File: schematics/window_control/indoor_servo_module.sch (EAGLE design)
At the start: 32 parts, among them J1 MTR-SERVO-FS5103B, J2 GND, J3 +5V, J4 OUTDOOR_SIGNAL, J5 J2, J6 J2, J7 J2, Q2 2N3904, Q3 2N3906BU, Q4 2N3904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

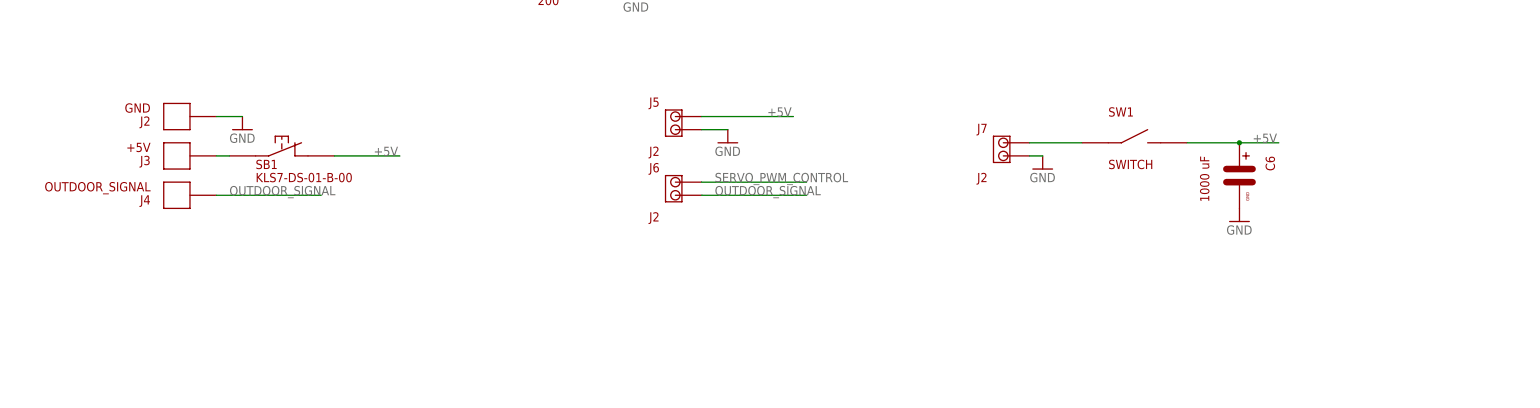
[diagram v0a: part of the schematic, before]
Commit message: Connectors changed
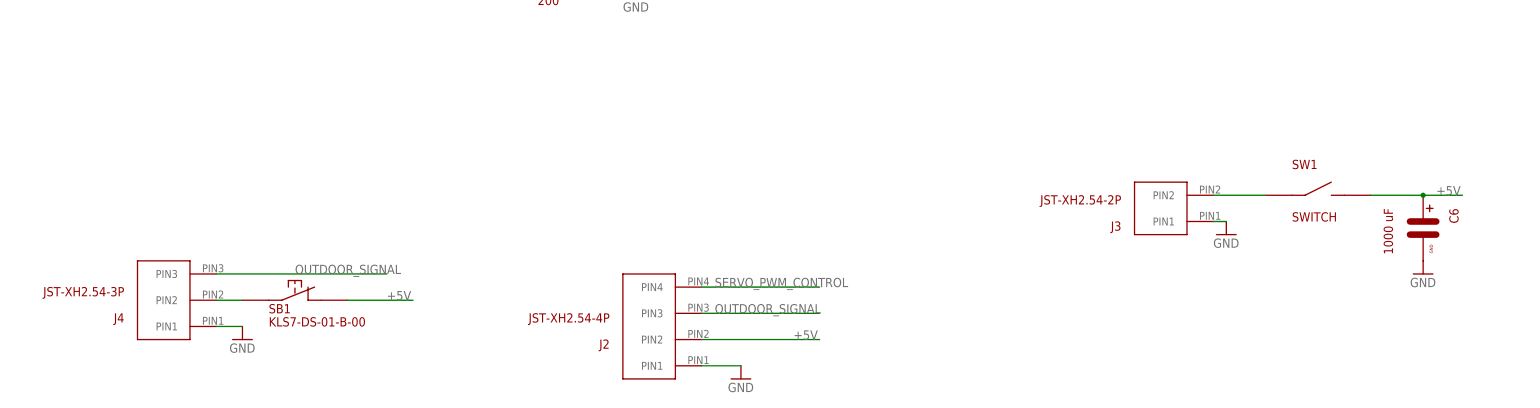
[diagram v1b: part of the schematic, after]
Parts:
- removed J5, J6, J7: J2, my_devices:J2
- J2: value GND -> JST-XH2.54-4P; device my_devices:J_SMD -> my_devices:JST-XH254-4P
- J3: value +5V -> JST-XH2.54-2P; device my_devices:J_SMD -> my_devices:JST-XH254-2P
- J4: value OUTDOOR_SIGNAL -> JST-XH2.54-3P; device my_devices:J_SMD -> my_devices:JST-XH254-3P
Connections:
- removed net N$5: J3.PIN, SB1.P$1
- new net N$4: J4.PIN2, SB1.P$1
- net +5V: now also J2.PIN2; no longer J5.PIN_1
- net GND: now also J2.PIN1, J3.PIN1, J4.PIN1; no longer J2.PIN, J5.PIN_2, J7.PIN_2
- net N$3: now also J3.PIN2; no longer J7.PIN_1
- net OUTDOOR_SIGNAL: now also J2.PIN3, J4.PIN3; no longer J4.PIN, J6.PIN_2
- net SERVO_PWM_CONTROL: now also J2.PIN4; no longer J6.PIN_1
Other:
- moved on the sheet: C6, SB1, SW1

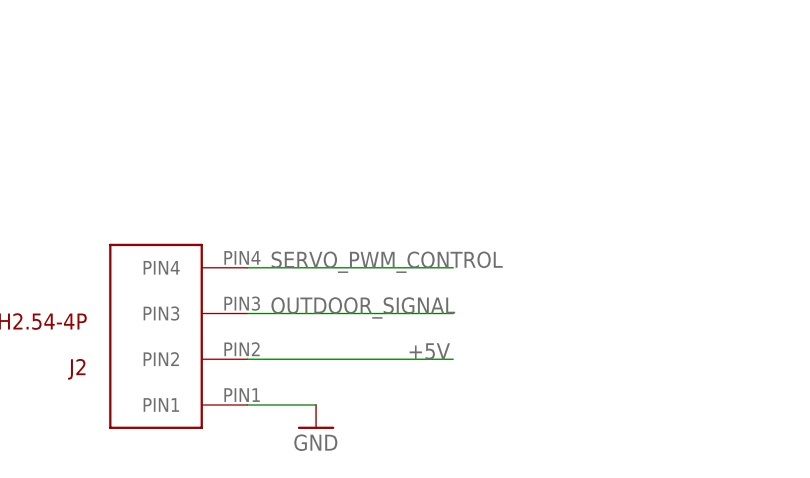
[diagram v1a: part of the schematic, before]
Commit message: Outdoor module board size reduced
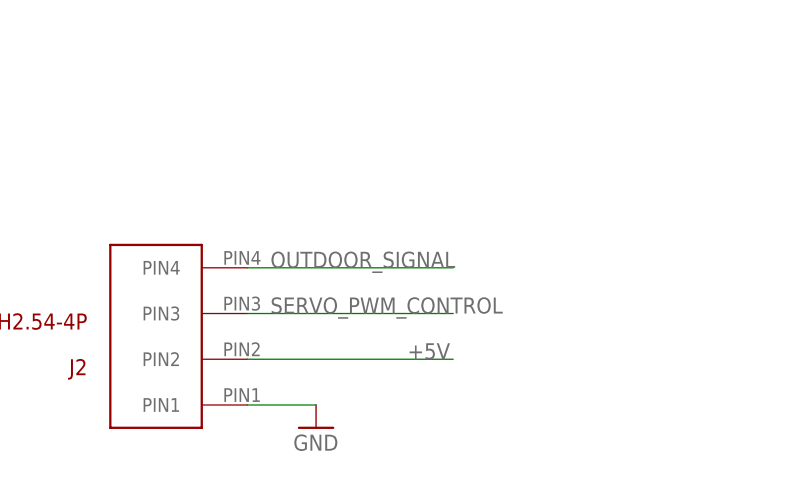
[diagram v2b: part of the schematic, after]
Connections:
- net OUTDOOR_SIGNAL: now also J2.PIN4; no longer J2.PIN3
- net SERVO_PWM_CONTROL: now also J2.PIN3; no longer J2.PIN4
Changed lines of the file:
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@@
 <grid distance="0.1" unitdist="inch" unit="inch" style="lines" multiple="1" display="no" altdistance="0.01" altunitdist="inch" altunit="inch"/>
 <layers>
-<layer number="1" name="Top" color="4" fill="1" visible="yes" active="no"/>
-<layer number="2" name="Route2" color="16" fill="1" visible="yes" active="no"/>
-<layer number="3" name="Route3" color="17" fill="1" visible="yes" active="no"/>
-<layer number="4" name="Route4" color="18" fill="1" visible="yes" active="no"/>
-<layer number="5" name="Route5" color="19" fill="1" visible="yes" active="no"/>
-<layer number="6" name="Route6" color="25" fill="1" visible="yes" active="no"/>
-<layer number="7" name="Route7" color="26" fill="1" visible="yes" active="no"/>
-<layer number="8" name="Route8" color="27" fill="1" visible="yes" active="no"/>
-<layer number="9" name="Route9" color="28" fill="1" visible="yes" active="no"/>
-<layer number="10" name="Route10" color="29" fill="1" visible="yes" active="no"/>
-<layer number="11" name="Route11" color="30" fill="1" visible="yes" active="no"/>
-<layer number="12" name="Route12" color="20" fill="1" visible="yes" active="no"/>
-<layer number="13" name="Route13" color="21" fill="1" visible="yes" active="no"/>
-<layer number="14" name="Route14" color="22" fill="1" visible="yes" active="no"/>
-<layer number="15" name="Route15" color="23" fill="1" visible="yes" active="no"/>
-<layer number="16" name="Bottom" color="1" fill="1" visible="yes" active="no"/>
-<layer number="17" name="Pads" color="2" fill="1" visible="yes" active="no"/>
-<layer number="18" name="Vias" color="2" fill="1" visible="yes" active="no"/>
-<layer number="19" name="Unrouted" color="6" fill="1" visible="yes" active="no"/>
-<layer number="20" name="Dimension" color="24" fill="1" visible="yes" active="no"/>
-<layer number="21" name="tPlace" color="7" fill="1" visible="yes" active="no"/>
-<layer number="22" name="bPlace" color="7" fill="1" visible="yes" active="no"/>
-<layer number="23" name="tOrigins" color="15" fill="1" visible="yes" active="no"/>
-<layer number="24" name="bOrigins" color="15" fill="1" visible="yes" active="no"/>
-<layer number="25" name="tNames" color="7" fill="1" visible="yes" active="no"/>
-<layer number="26" name="bNames" color="7" fill="1" visible="yes" active="no"/>
-<layer number="27" name="tValues" color="7" fill="1" visible="yes" active="no"/>
-<layer number="28" name="bValues" color="7" fill="1" visible="yes" active="no"/>
+<layer number="1" name="Top" color="4" fill="1" visible="no" active="no"/>
+<layer number="2" name="Route2" color="16" fill="1" visible="no" active="no"/>
+<layer number="3" name="Route3" color="17" fill="1" visible="no" active="no"/>
+<layer number="4" name="Route4" color="18" fill="1" visible="no" active="no"/>
+<layer number="5" name="Route5" color="19" fill="1" visible="no" active="no"/>
+<layer number="6" name="Route6" color="25" fill="1" visible="no" active="no"/>
+<layer number="7" name="Route7" color="26" fill="1" visible="no" active="no"/>
+<layer number="8" name="Route8" color="27" fill="1" visible="no" active="no"/>
+<layer number="9" name="Route9" color="28" fill="1" visible="no" active="no"/>
+<layer number="10" name="Route10" color="29" fill="1" visible="no" active="no"/>
+<layer number="11" name="Route11" color="30" fill="1" visible="no" active="no"/>
+<layer number="12" name="Route12" color="20" fill="1" visible="no" active="no"/>
+<layer number="13" name="Route13" color="21" fill="1" visible="no" active="no"/>
+<layer number="14" name="Route14" color="22" fill="1" visible="no" active="no"/>
+<layer number="15" name="Route15" color="23" fill="1" visible="no" active="no"/>
+<layer number="16" name="Bottom" color="1" fill="1" visible="no" active="no"/>
+<layer number="17" name="Pads" color="2" fill="1" visible="no" active="no"/>
+<layer number="18" name="Vias" color="2" fill="1" visible="no" active="no"/>
+<layer number="19" name="Unrouted" color="6" fill="1" visible="no" active="no"/>
+<layer number="20" name="Dimension" color="24" fill="1" visible="no" active="no"/>
+<layer number="21" name="tPlace" color="7" fill="1" visible="no" active="no"/>
+<layer number="22" name="bPlace" color="7" fill="1" visible="no" active="no"/>
+<layer number="23" name="tOrigins" color="15" fill="1" visible="no" active="no"/>
+<layer number="24" name="bOrigins" color="15" fill="1" visible="no" active="no"/>
+<layer number="25" name="tNames" color="7" fill="1" visible="no" active="no"/>
+<layer number="26" name="bNames" color="7" fill="1" visible="no" active="no"/>
+<layer number="27" name="tValues" color="7" fill="1" visible="no" active="no"/>
+<layer number="28" name="bValues" color="7" fill="1" visible="no" active="no"/>
 <layer number="29" name="tStop" color="7" fill="3" visible="no" active="no"/>
 <layer number="30" name="bStop" color="7" fill="6" visible="no" active="no"/>
@@
 <layer number="35" name="tGlue" color="7" fill="4" visible="no" active="no"/>
 <layer number="36" name="bGlue" color="7" fill="5" visible="no" active="no"/>
-<layer number="37" name="tTest" color="7" fill="1" visible="yes" active="no"/>
-<layer number="38" name="bTest" color="7" fill="1" visible="yes" active="no"/>
+<layer number="37" name="tTest" color="7" fill="1" visible="no" active="no"/>
+<layer number="38" name="bTest" color="7" fill="1" visible="no" active="no"/>
 <layer number="39" name="tKeepout" color="4" fill="11" visible="no" active="no"/>
 <layer number="40" name="bKeepout" color="1" fill="11" visible="no" active="no"/>
@@
 <layer number="44" name="Drills" color="7" fill="1" visible="no" active="no"/>
 <layer number="45" name="Holes" color="7" fill="1" visible="no" active="no"/>
-<layer number="46" name="Milling" color="3" fill="1" visible="yes" active="no"/>
-<layer number="47" name="Measures" color="7" fill="1" visible="yes" active="no"/>
-<layer number="48" name="Document" color="7" fill="1" visible="yes" active="no"/>
-<layer number="49" name="Reference" color="7" fill="1" visible="yes" active="no"/>
-<layer number="51" name="tDocu" color="7" fill="1" visible="yes" active="no"/>
-<layer number="52" name="bDocu" color="7" fill="1" visible="yes" active="no"/>
+<layer number="46" name="Milling" color="3" fill="1" visible="no" active="no"/>
+<layer number="47" name="Measures" color="7" fill="1" visible="no" active="no"/>
+<layer number="48" name="Document" color="7" fill="1" visible="no" active="no"/>
+<layer number="49" name="Reference" color="7" fill="1" visible="no" active="no"/>
+<layer number="51" name="tDocu" color="7" fill="1" visible="no" active="no"/>
+<layer number="52" name="bDocu" color="7" fill="1" visible="no" active="no"/>
 <layer number="88" name="SimResults" color="9" fill="1" visible="yes" active="yes"/>
 <layer number="89" name="SimProbes" color="9" fill="1" visible="yes" active="yes"/>
@@
 </segment>
 <segment>
-<pinref part="J2" gate="G$1" pin="PIN4"/>
-<wire x1="-5.08" y1="-68.58" x2="17.78" y2="-68.58" width="0.1524" layer="91" grouprefs="NEAR_HANDLE_MODULE_CONNECTOR"/>
-<label x="-2.54" y="-68.58" size="1.778" layer="95" grouprefs="NEAR_HANDLE_MODULE_CONNECTOR"/>
+<pinref part="J2" gate="G$1" pin="PIN3"/>
+<wire x1="-5.08" y1="-73.66" x2="17.78" y2="-73.66" width="0.1524" layer="91" grouprefs="NEAR_HANDLE_MODULE_CONNECTOR"/>
+<label x="-2.54" y="-73.66" size="1.778" layer="95" grouprefs="NEAR_HANDLE_MODULE_CONNECTOR"/>
 </segment>
 </net>
@@
 </segment>
 <segment>
-<pinref part="J2" gate="G$1" pin="PIN3"/>
-<wire x1="-5.08" y1="-73.66" x2="17.78" y2="-73.66" width="0.1524" layer="91" grouprefs="NEAR_HANDLE_MODULE_CONNECTOR"/>
-<label x="-2.54" y="-73.66" size="1.778" layer="95" grouprefs="NEAR_HANDLE_MODULE_CONNECTOR"/>
-</segment>
-</net>
+<pinref part="J2" gate="G$1" pin="PIN4"/>
+<wire x1="-5.08" y1="-68.58" x2="17.78" y2="-68.58" width="0.1524" layer="91" grouprefs="NEAR_HANDLE_MODULE_CONNECTOR"/>
+<label x="-2.54" y="-68.58" size="1.778" layer="95" grouprefs="NEAR_HANDLE_MODULE_CONNECTOR"/>
+</segment>
+</net>
